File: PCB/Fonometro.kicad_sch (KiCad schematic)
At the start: 53 parts, among them J1 Conn_01x15_Male, J2 Conn_01x15_Male, U1 LM324, U2 LM358, U3 ESP32-DEVKIT-V1

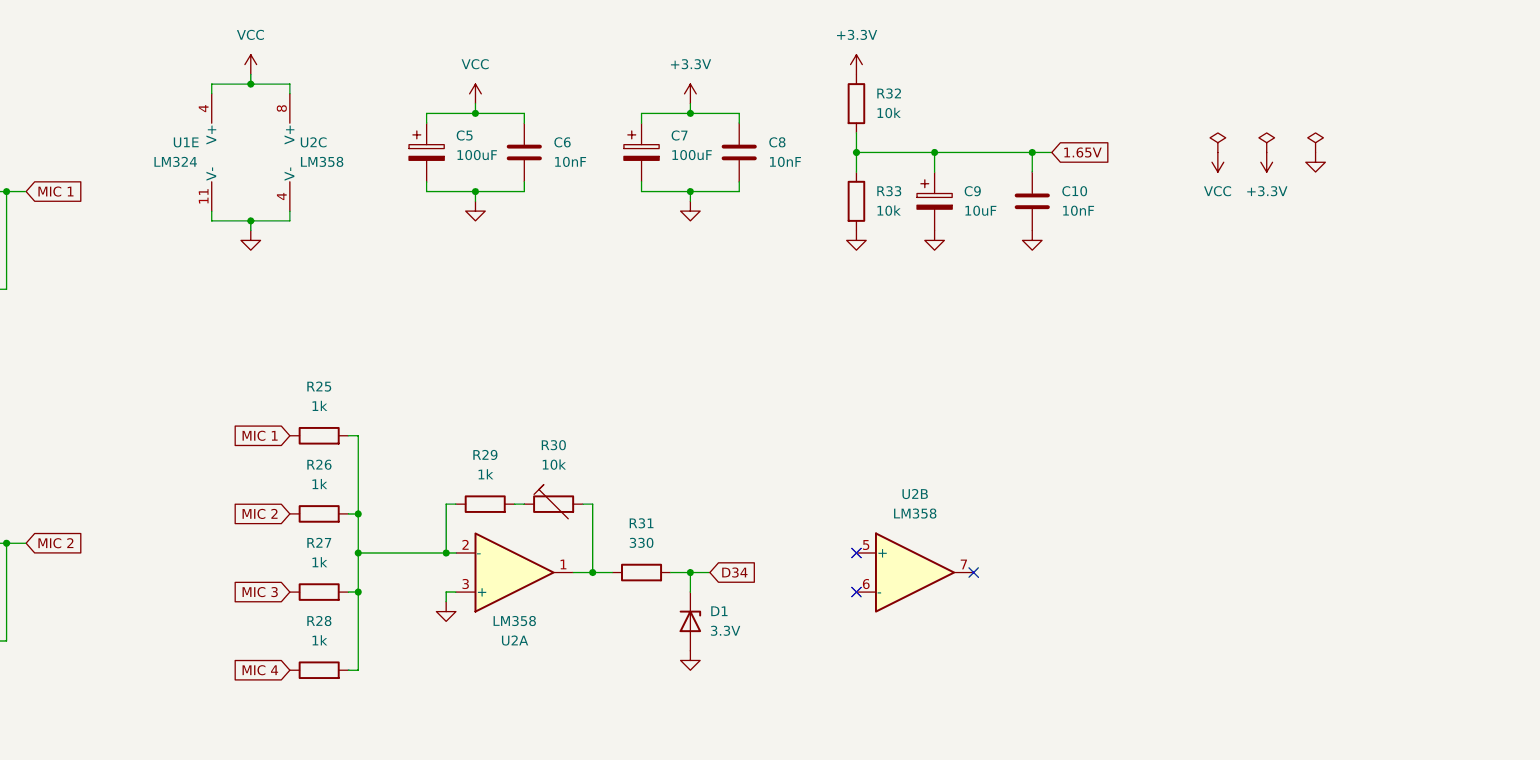
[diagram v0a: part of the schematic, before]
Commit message: feat: added power part and first PCB release.
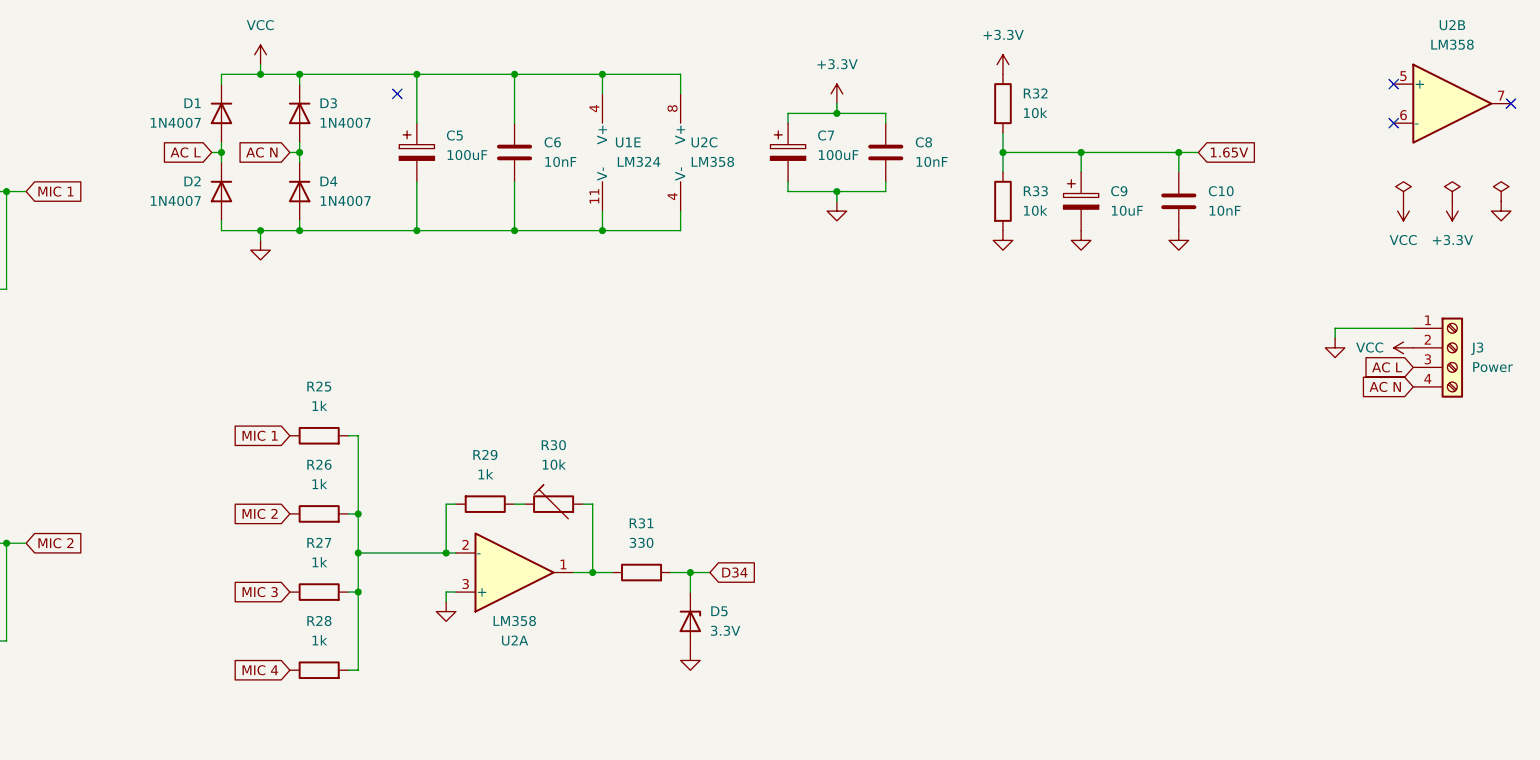
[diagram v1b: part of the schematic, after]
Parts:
- removed D1: 3.3V, symbol Device:D_Zener
- added D1, D2, D3, D4: 1N4007, Diode_THT:D_DO-41_SOD81_P7.62mm_Horizontal, symbol Diode:1N4007
- added D5: 3.3V, Diode_THT:D_DO-41_SOD81_P7.62mm_Horizontal, symbol Device:D_Zener
- added J3: Power, TerminalBlock_4Ucon:TerminalBlock_4Ucon_1x04_P3.50mm_Horizontal, symbol Connector:Screw_Terminal_01x04
- C1, C2, C3, C4, C9: footprint (none) -> Capacitor_THT:CP_Radial_D4.0mm_P1.50mm
- C10, C6, C8: footprint (none) -> Capacitor_THT:C_Rect_L7.0mm_W2.5mm_P5.00mm
- C5, C7: footprint (none) -> Capacitor_THT:CP_Radial_D6.3mm_P2.50mm
- J1, J2: footprint (none) -> Connector_PinHeader_2.54mm:PinHeader_1x15_P2.54mm_Vertical
- MK1, MK2, MK3, MK4: footprint (none) -> Connector_PinHeader_2.54mm:PinHeader_1x02_P2.54mm_Vertical
- R1, R10, R11, R12, R13, R14, R15, R16, R17, R18, R19, R20, R21, R22, R23, R24, R25, R26, R27, R28, R29, R3, R31, R32, R33, R5, R7, R9: footprint (none) -> Resistor_THT:R_Axial_DIN0207_L6.3mm_D2.5mm_P7.62mm_Horizontal
- R2, R30, R4, R6, R8: footprint (none) -> Potentiometer_THT:Potentiometer_Runtron_RM-065_Vertical
- U1: footprint (none) -> Package_DIP:DIP-14_W7.62mm_Socket
- U2: footprint (none) -> Package_DIP:DIP-8_W7.62mm_Socket
- U3: footprint (none) -> ESP32-DEVKIT-V1:MODULE_ESP32_DEVKIT_V1
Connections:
- net D34: now also D5.1 (K)
- net GND: now also D2.2 (A), D4.2 (A), D5.2 (A), J3.1 (Pin_1)
- net VCC: now also D1.1 (K), D3.1 (K), J3.2 (Pin_2)
- net at R30.1: now also R29.1; no longer R29.2
- net at R25.2, R26.2, R27.2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: now also R29.2; no longer R29.1
- new net AC L: D1.2 (A), D2.1 (K), J3.3 (Pin_3)
- new net AC N: D3.2 (A), D4.1 (K), J3.4 (Pin_4)
- no-connect marks 3 -> 4
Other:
- moved on the sheet: C10, C5, C6, C7, C8, C9, R29, R32, R33, U1E, U2B, U2C

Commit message: feat: improved PCB layout.
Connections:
- net MIC 2: now also R22.1; no longer R22.2
- net MIC 4: now also R24.1; no longer R24.2
- net at R20.2, U1.13 (-): now also R24.2; no longer R24.1
- net at R18.2, U1.6 (-): now also R22.2; no longer R22.1
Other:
- moved on the sheet: R22, R24
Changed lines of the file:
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@@
     (pin "1")
   )
-  (symbol (lib_id "Device:R") (at 73.66 96.52 90) (unit 1)
+  (symbol (lib_id "Device:R") (at 73.66 96.52 270) (unit 1)
     (in_bom yes) (on_board yes) (fields_autoplaced)
     (property "Reference" "R22" (id 0) (at 73.66 90.17 90))
     (property "Value" "1M" (id 1) (at 73.66 92.71 90))
-    (property "Footprint" "Resistor_THT:R_Axial_DIN0207_L6.3mm_D2.5mm_P7.62mm_Horizontal" (id 2) (at 73.66 98.298 90)
+    (property "Footprint" "Resistor_THT:R_Axial_DIN0207_L6.3mm_D2.5mm_P7.62mm_Horizontal" (id 2) (at 73.66 94.742 90)
       (effects (font (size 1.27 1.27)) hide)
     )
@@
     (pin "2")
   )
-  (symbol (lib_id "Device:R") (at 73.66 187.96 90) (unit 1)
+  (symbol (lib_id "Device:R") (at 73.66 187.96 270) (unit 1)
     (in_bom yes) (on_board yes) (fields_autoplaced)
     (property "Reference" "R24" (id 0) (at 73.66 181.61 90))
     (property "Value" "1M" (id 1) (at 73.66 184.15 90))
-    (property "Footprint" "Resistor_THT:R_Axial_DIN0207_L6.3mm_D2.5mm_P7.62mm_Horizontal" (id 2) (at 73.66 189.738 90)
+    (property "Footprint" "Resistor_THT:R_Axial_DIN0207_L6.3mm_D2.5mm_P7.62mm_Horizontal" (id 2) (at 73.66 186.182 90)
       (effects (font (size 1.27 1.27)) hide)
     )

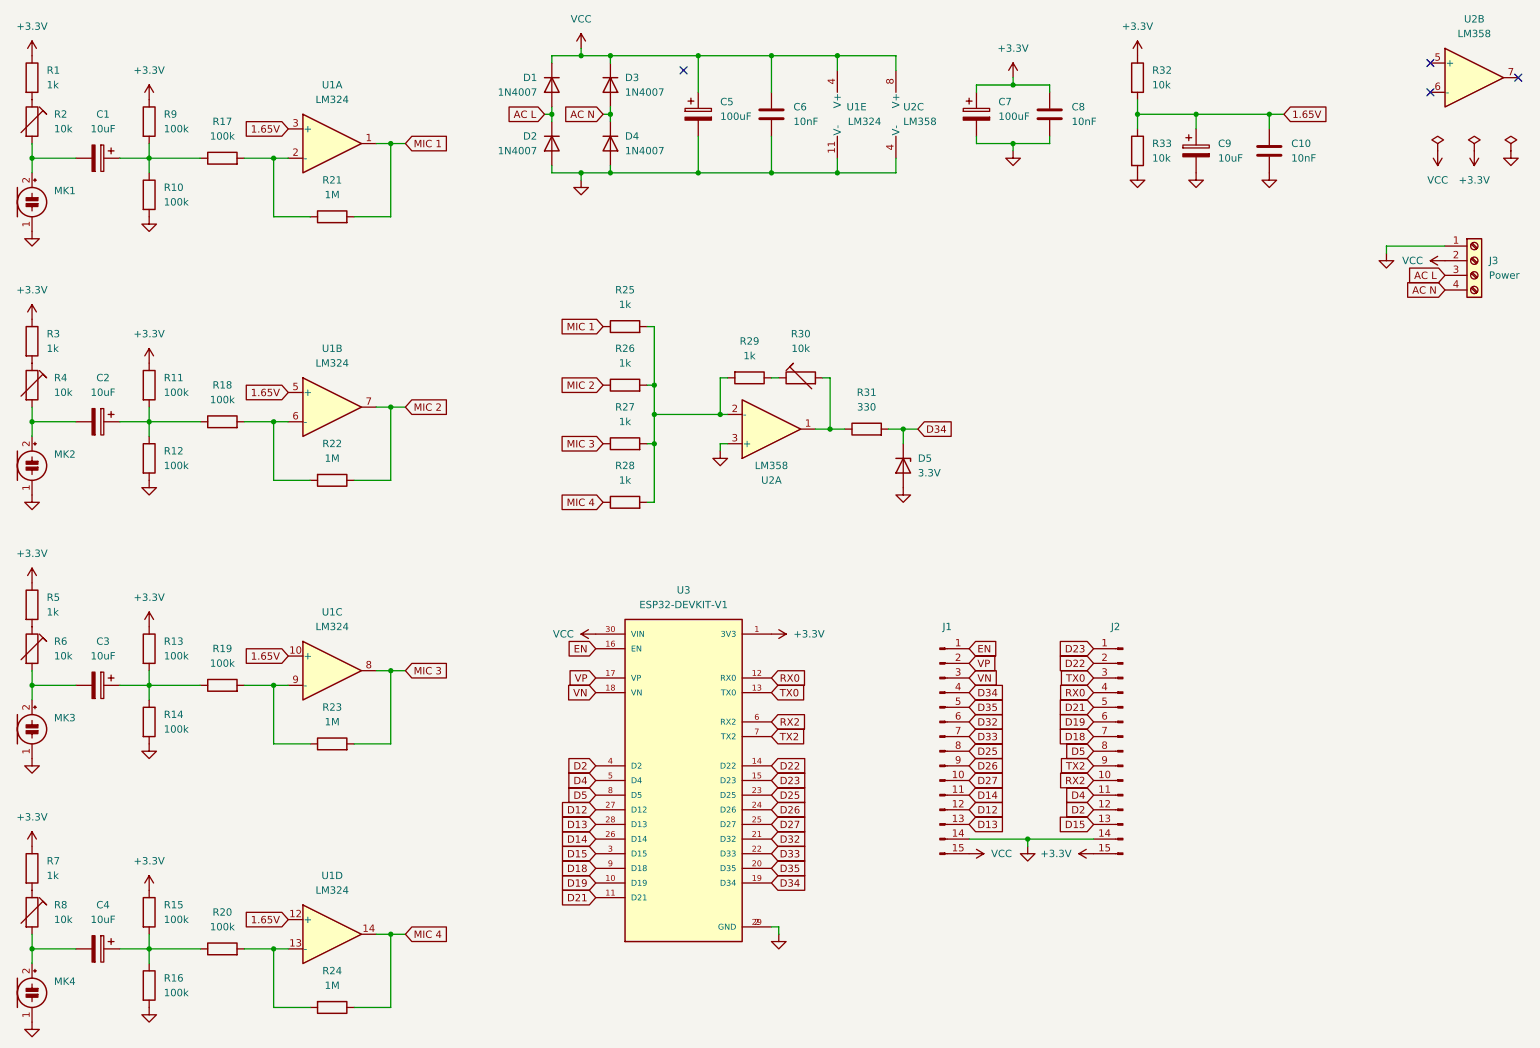
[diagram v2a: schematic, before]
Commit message: feat: added single channel ADC input on MCU.
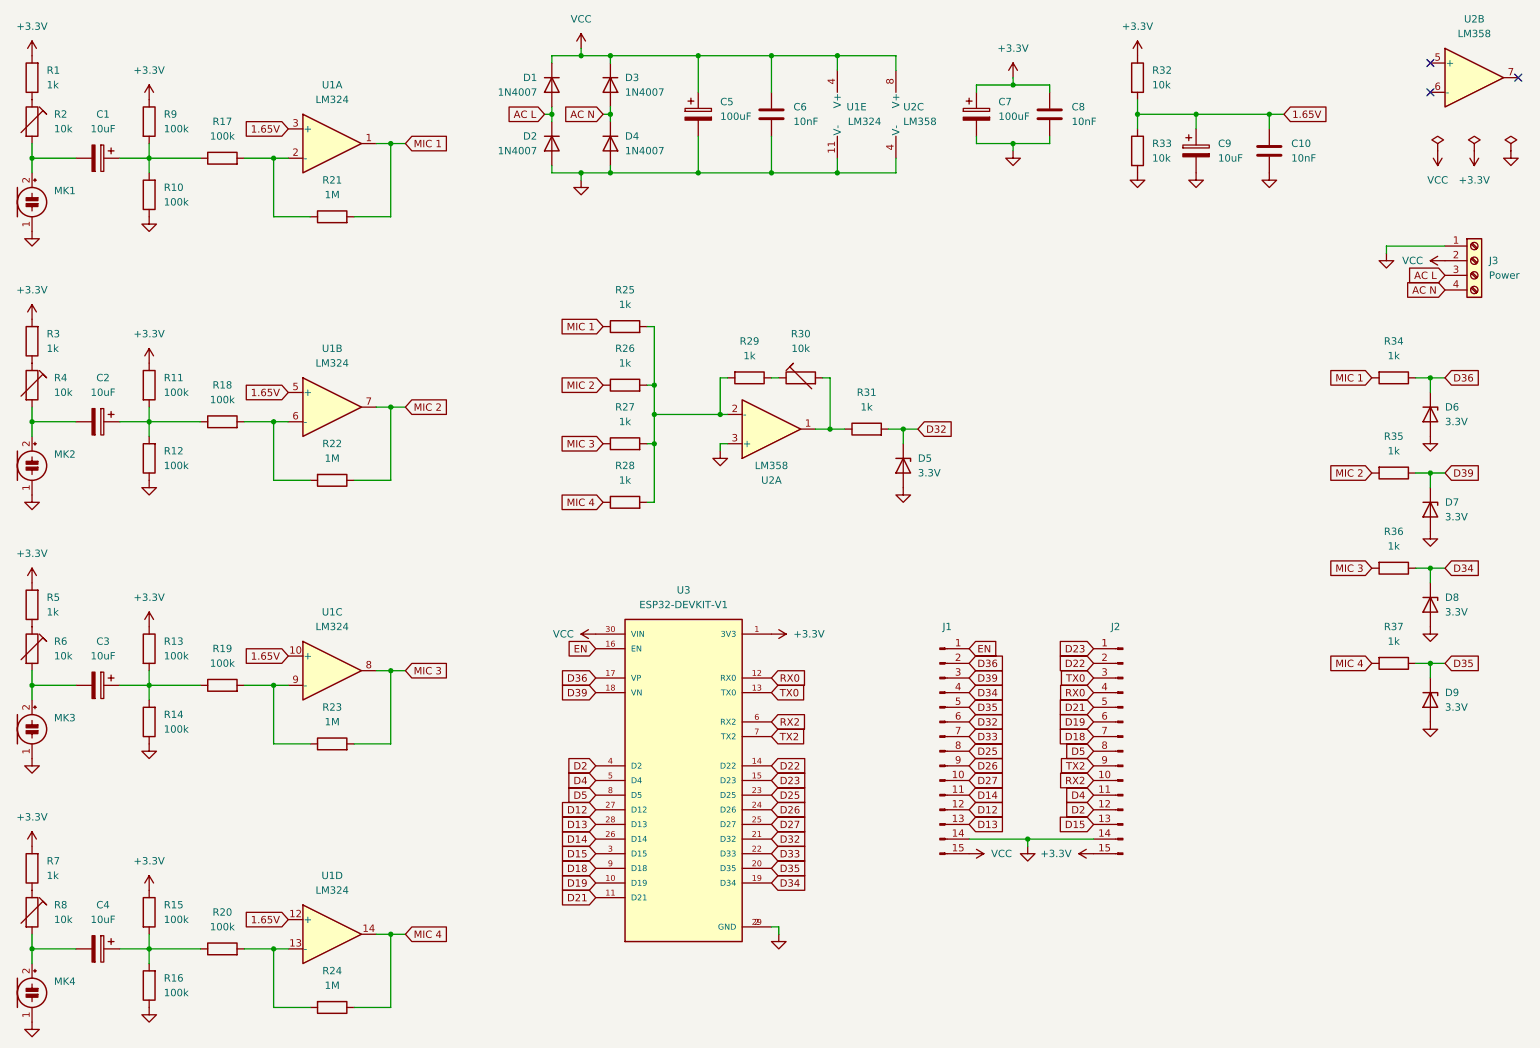
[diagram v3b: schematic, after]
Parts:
- added D6, D7, D8, D9: 3.3V, Diode_THT:D_DO-41_SOD81_P7.62mm_Horizontal, symbol Device:D_Zener
- added R34, R35, R36, R37: 1k, Resistor_THT:R_Axial_DIN0207_L6.3mm_D2.5mm_P7.62mm_Horizontal, symbol Device:R
- R31: value 330 -> 1k
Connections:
- net +3V3: now also R1.2, R3.2, R5.2, R7.2; no longer R1.1, R3.1, R5.1, R7.1
- net D32: now also D5.1 (K), R31.2
- net D34: now also D8.1 (K), R36.1; no longer D5.1 (K), R31.2
- net D35: now also D9.1 (K), R37.1
- net GND: now also R10.1, R12.1, R14.1, R16.1, D6.2 (A), D7.2 (A), D8.2 (A), D9.2 (A); no longer R10.2, R12.2, R14.2, R16.2
- net MIC 1: now also R34.2
- net MIC 2: now also R35.2
- net MIC 3: now also R36.2
- net MIC 4: now also R37.2
- net at C3.1, R13.2, R19.1: now also R14.2; no longer R14.1
- net at R2.1: now also R1.1; no longer R1.2
- net at R8.1: now also R7.1; no longer R7.2
- net at C1.1, R17.1, R9.2: now also R10.2; no longer R10.1
- net at C2.1, R11.2, R18.1: now also R12.2; no longer R12.1
- net at C4.1, R15.2, R20.1: now also R16.2; no longer R16.1
- net at R6.1: now also R5.1; no longer R5.2
- net at R4.1: now also R3.1; no longer R3.2
- net VN renamed D39
- net D39: now also D7.1 (K), R35.1
- net VP renamed D36
- net D36: now also D6.1 (K), R34.1
- no-connect marks 4 -> 3
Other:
- moved on the sheet: R1, R10, R12, R14, R16, R3, R5, R7

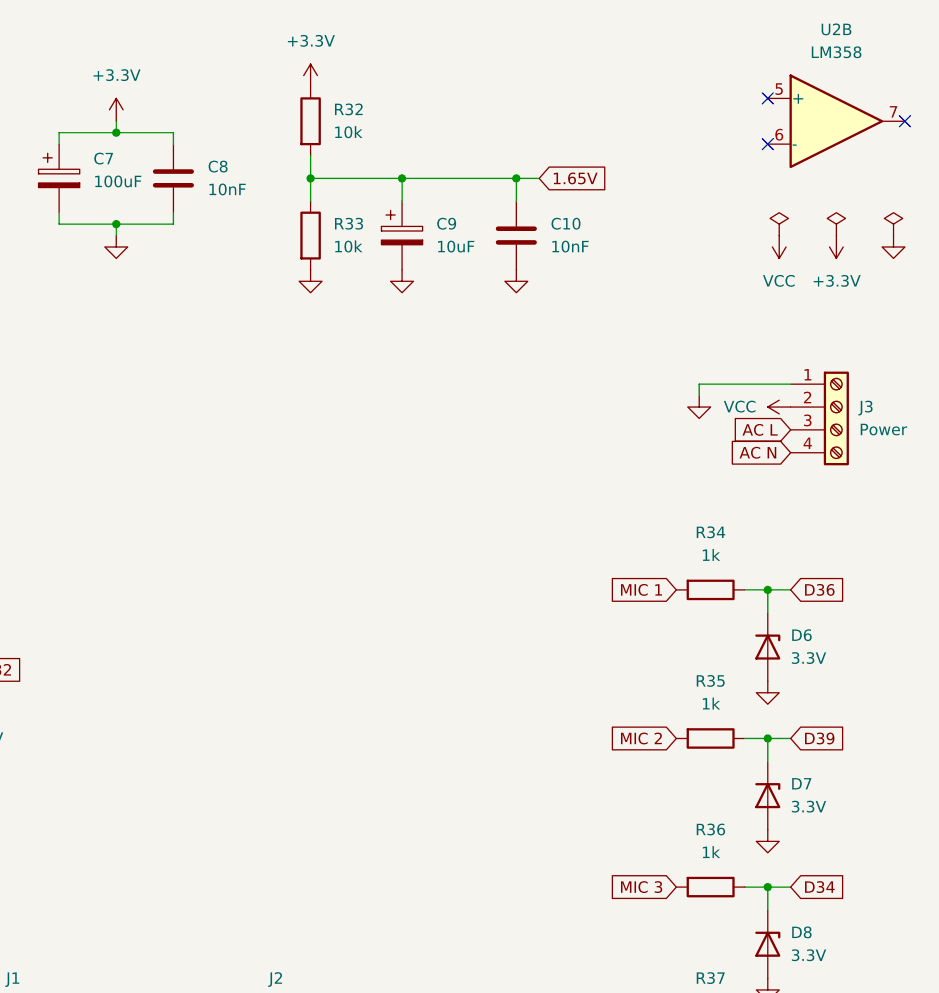
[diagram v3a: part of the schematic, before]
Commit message: feat: J4 and J5 for U2B.
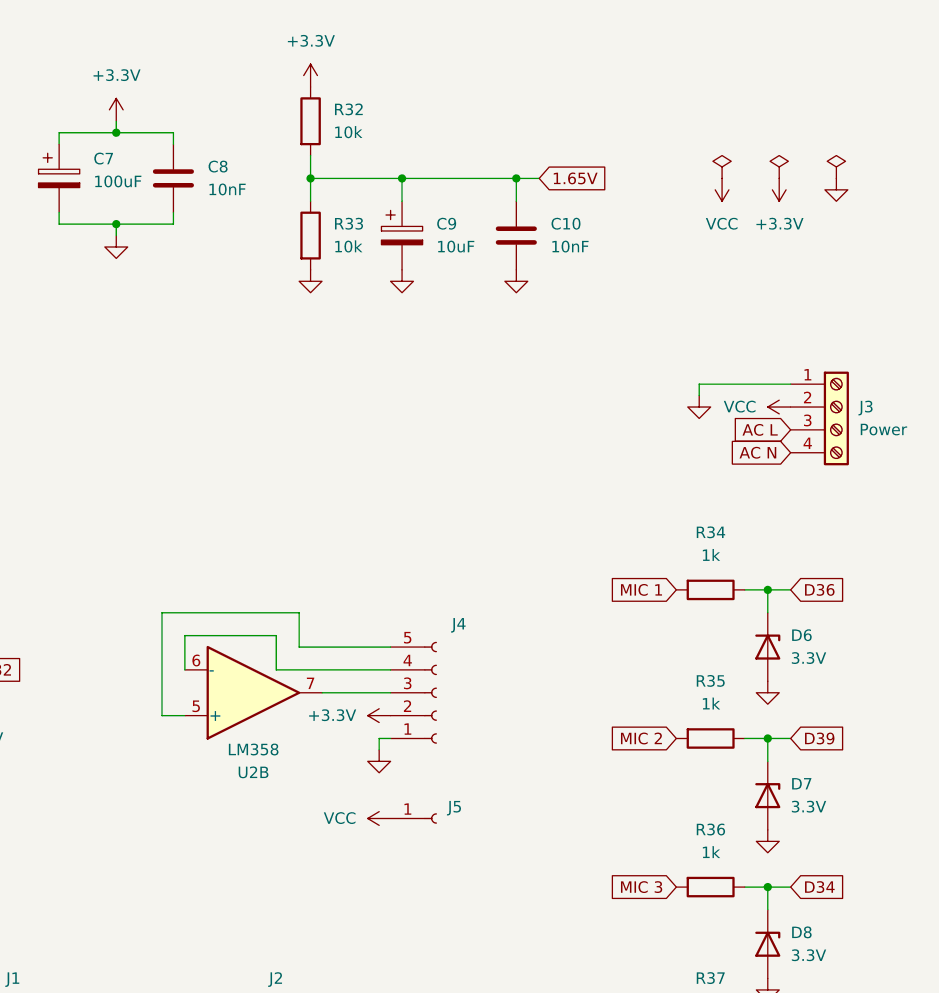
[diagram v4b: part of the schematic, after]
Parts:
- added J4: Conn_01x05_Female, Connector_PinHeader_2.54mm:PinHeader_1x05_P2.54mm_Vertical, symbol Connector:Conn_01x05_Female
- added J5: Conn_01x01_Female, Connector_PinHeader_2.54mm:PinHeader_1x01_P2.54mm_Vertical, symbol Connector:Conn_01x01_Female
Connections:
- net +3V3: now also J4.2 (Pin_2)
- net GND: now also J4.1 (Pin_1)
- net VCC: now also J5.1 (Pin_1)
- net at U2.5 (+): now also J4.5 (Pin_5)
- net at U2.6 (-): now also J4.4 (Pin_4)
- net at U2.7: now also J4.3 (Pin_3)
- no-connect marks 3 -> 0
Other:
- moved on the sheet: U2B
